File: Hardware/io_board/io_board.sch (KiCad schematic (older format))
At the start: 31 parts, among them J1 Conn_01x40, J2 Conn_02x05_Odd_Even, J3 Mini-DIN-6, J4 Conn_02x10_Odd_Even, U1 74LS138, U2 W65C22NxP, U3 74LS14

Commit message: Make IO board through hole
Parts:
- removed J2: Conn_02x05_Odd_Even, Connector_PinHeader_2.54mm:PinHeader_2x07_P2.54mm_Horizontal, symbol Connector_Generic:Conn_02x07_Odd_Even
- added J2: Conn_02x06_Odd_Even, Connector_PinHeader_2.54mm:PinHeader_2x06_P2.54mm_Horizontal, symbol Connector_Generic:Conn_02x06_Odd_Even
- C1, C2, C3, C4: value C_Small -> 4.7u; footprint Capacitor_SMD:C_1206_3216Metric_Pad1.42x1.75mm_HandSolder -> Capacitor_THT:C_Disc_D4.7mm_W2.5mm_P5.00mm
- D1, D2, D3, D4, D5, D6, D7, D8: footprint LED_SMD:LED_1206_3216Metric_Pad1.42x1.75mm_HandSolder -> LED_THT:LED_D3.0mm_Horizontal_O3.81mm_Z6.0mm
- R1, R10, R11, R12, R2, R3, R4, R5, R6, R7, R8, R9: footprint Resistor_SMD:R_0805_2012Metric_Pad1.15x1.40mm_HandSolder -> Resistor_THT:R_Axial_DIN0204_L3.6mm_D1.6mm_P5.08mm_Horizontal
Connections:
- net +5V: now also J2.2 (Pin_2)
- net CA1: now also J2.6 (Pin_6)
- net CA2: now also J2.4 (Pin_4)
- net GND: now also C2.2, J2.8 (Pin_8)
- net PA0: now also J2.11 (Pin_11)
- net PA1: now also J2.9 (Pin_9)
- net PA2: now also J2.7 (Pin_7)
- net PA3: now also J2.5 (Pin_5)
- net PA4: now also J2.3 (Pin_3)
- net PA5: now also J2.1 (Pin_1)
- net PA6: now also J2.12 (Pin_12)
- net PA7: now also J2.10 (Pin_10)
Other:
- moved on the sheet: U3F

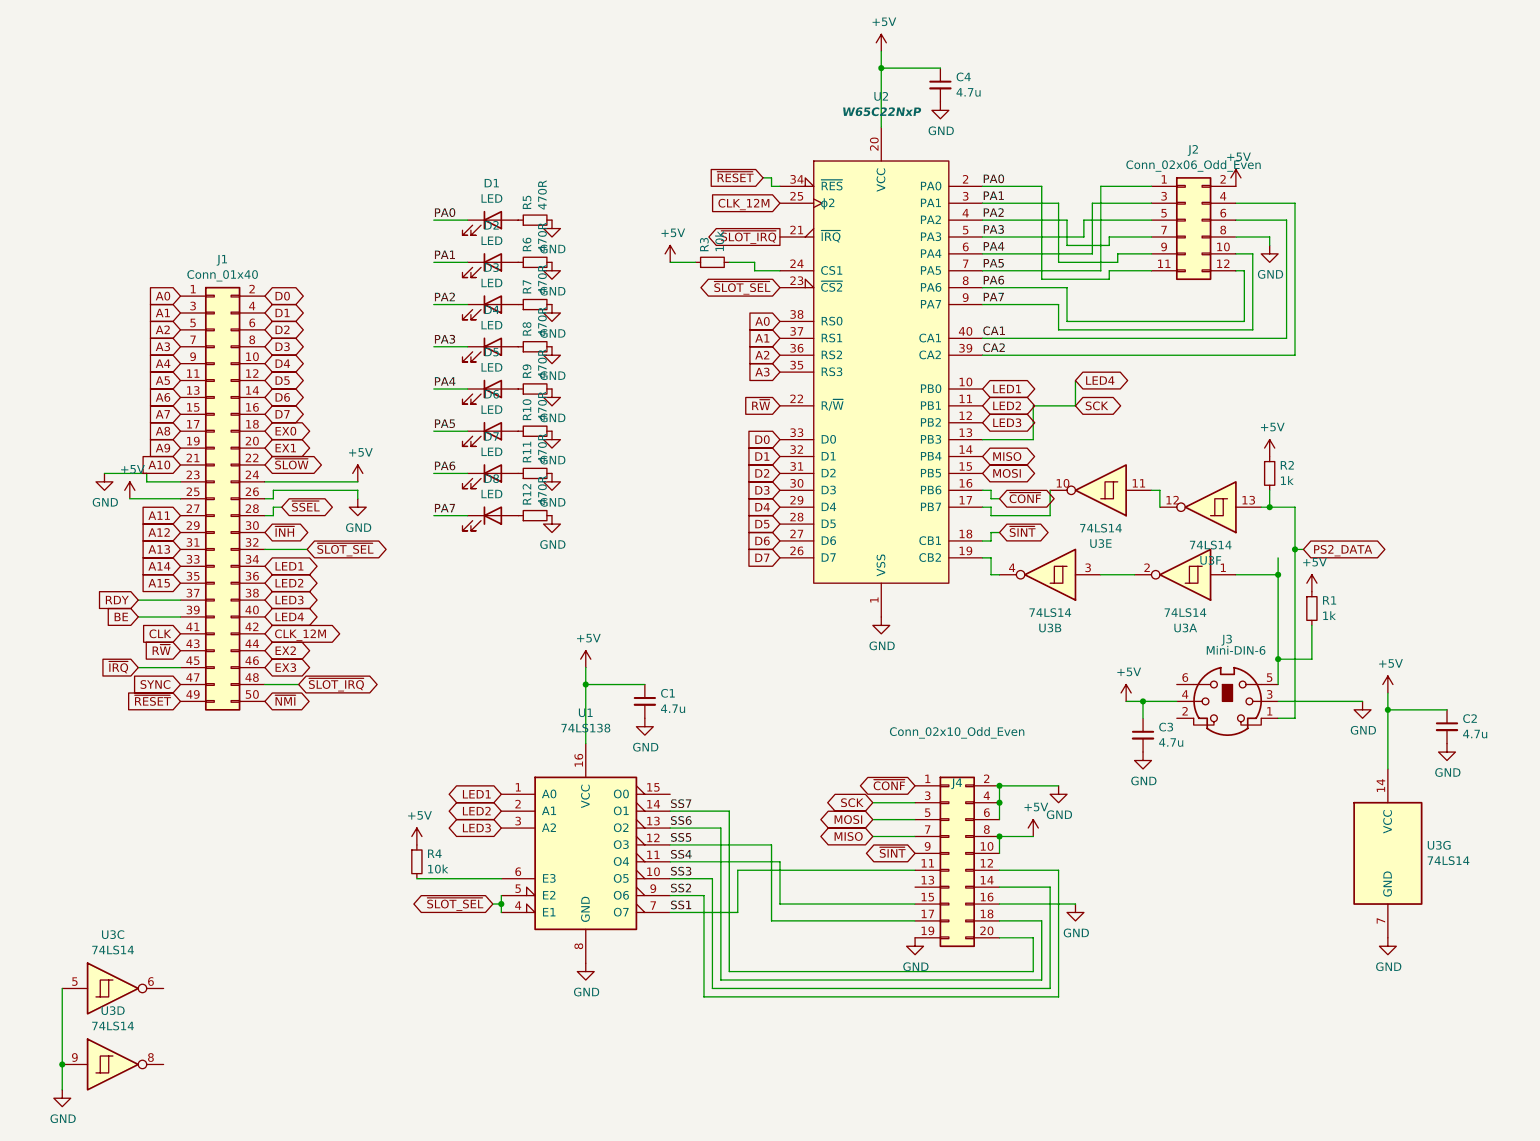
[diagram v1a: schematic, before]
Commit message: final update for through hole conversion
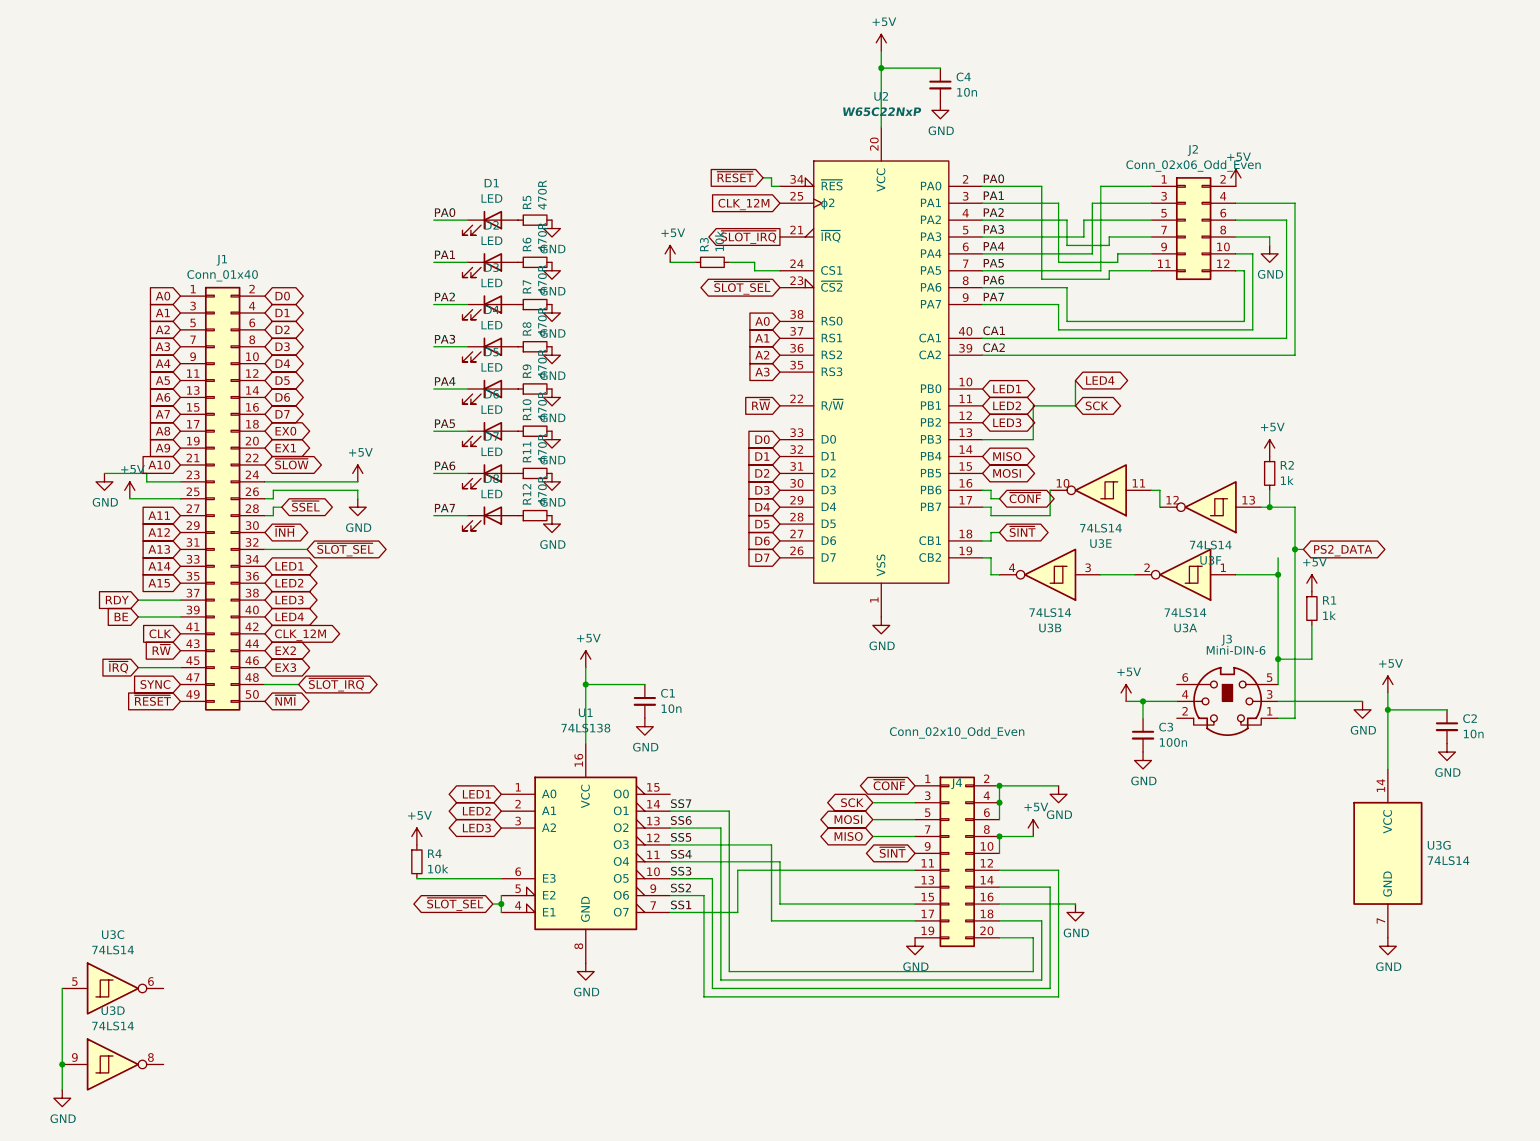
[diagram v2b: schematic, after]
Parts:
- C1, C2, C4: value 4.7u -> 10n
- C3: value 4.7u -> 100n
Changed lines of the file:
@@
 P 6800 1000
 F 0 "C4" H 6892 1046 50  0000 L CNN
-F 1 "4.7u" H 6892 955 50  0000 L CNN
+F 1 "10n" H 6892 955 50  0000 L CNN
 F 2 "Capacitor_THT:C_Disc_D4.7mm_W2.5mm_P5.00mm" H 6800 1000 50  0001 C CNN
 F 3 "~" H 6800 1000 50  0001 C CNN
@@
 P 5050 4650
 F 0 "C1" H 5142 4696 50  0000 L CNN
-F 1 "4.7u" H 5142 4605 50  0000 L CNN
+F 1 "10n" H 5142 4605 50  0000 L CNN
 F 2 "Capacitor_THT:C_Disc_D4.7mm_W2.5mm_P5.00mm" H 5050 4650 50  0001 C CNN
 F 3 "~" H 5050 4650 50  0001 C CNN
@@
 P 9800 4800
 F 0 "C2" H 9892 4846 50  0000 L CNN
-F 1 "4.7u" H 9892 4755 50  0000 L CNN
+F 1 "10n" H 9892 4755 50  0000 L CNN
 F 2 "Capacitor_THT:C_Disc_D4.7mm_W2.5mm_P5.00mm" H 9800 4800 50  0001 C CNN
 F 3 "~" H 9800 4800 50  0001 C CNN
@@
 P 8000 4850
 F 0 "C3" H 8092 4896 50  0000 L CNN
-F 1 "4.7u" H 8092 4805 50  0000 L CNN
+F 1 "100n" H 8092 4805 50  0000 L CNN
 F 2 "Capacitor_THT:C_Disc_D4.7mm_W2.5mm_P5.00mm" H 8000 4850 50  0001 C CNN
 F 3 "~" H 8000 4850 50  0001 C CNN

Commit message: update io board with bigger resistors
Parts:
- R1, R10, R11, R12, R2, R3, R4, R5, R6, R7, R8, R9: footprint Resistor_THT:R_Axial_DIN0204_L3.6mm_D1.6mm_P5.08mm_Horizontal -> Resistor_THT:R_Axial_DIN0207_L6.3mm_D2.5mm_P7.62mm_Horizontal
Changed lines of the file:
@@
 F 0 "R2" H 8809 3346 50  0000 L CNN
 F 1 "1k" H 8809 3255 50  0000 L CNN
-F 2 "Resistor_THT:R_Axial_DIN0204_L3.6mm_D1.6mm_P5.08mm_Horizontal" H 8750 3300 50  0001 C CNN
+F 2 "Resistor_THT:R_Axial_DIN0207_L6.3mm_D2.5mm_P7.62mm_Horizontal" H 8750 3300 50  0001 C CNN
 F 3 "~" H 8750 3300 50  0001 C CNN
 	1    8750 3300
@@
 F 0 "R1" H 9059 4146 50  0000 L CNN
 F 1 "1k" H 9059 4055 50  0000 L CNN
-F 2 "Resistor_THT:R_Axial_DIN0204_L3.6mm_D1.6mm_P5.08mm_Horizontal" H 9000 4100 50  0001 C CNN
+F 2 "Resistor_THT:R_Axial_DIN0207_L6.3mm_D2.5mm_P7.62mm_Horizontal" H 9000 4100 50  0001 C CNN
 F 3 "~" H 9000 4100 50  0001 C CNN
 	1    9000 4100
@@
 F 0 "R3" H 5509 2096 50  0000 L CNN
 F 1 "10k" H 5509 2005 50  0000 L CNN
-F 2 "Resistor_THT:R_Axial_DIN0204_L3.6mm_D1.6mm_P5.08mm_Horizontal" H 5450 2050 50  0001 C CNN
+F 2 "Resistor_THT:R_Axial_DIN0207_L6.3mm_D2.5mm_P7.62mm_Horizontal" H 5450 2050 50  0001 C CNN
 F 3 "~" H 5450 2050 50  0001 C CNN
 	1    5450 2050
@@
 F 0 "R4" H 3759 5646 50  0000 L CNN
 F 1 "10k" H 3759 5555 50  0000 L CNN
-F 2 "Resistor_THT:R_Axial_DIN0204_L3.6mm_D1.6mm_P5.08mm_Horizontal" H 3700 5600 50  0001 C CNN
+F 2 "Resistor_THT:R_Axial_DIN0207_L6.3mm_D2.5mm_P7.62mm_Horizontal" H 3700 5600 50  0001 C CNN
 F 3 "~" H 3700 5600 50  0001 C CNN
 	1    3700 5600
@@
 F 0 "R5" H 4459 1846 50  0000 L CNN
 F 1 "470R" H 4459 1755 50  0000 L CNN
-F 2 "Resistor_THT:R_Axial_DIN0204_L3.6mm_D1.6mm_P5.08mm_Horizontal" H 4400 1800 50  0001 C CNN
+F 2 "Resistor_THT:R_Axial_DIN0207_L6.3mm_D2.5mm_P7.62mm_Horizontal" H 4400 1800 50  0001 C CNN
 F 3 "~" H 4400 1800 50  0001 C CNN
 	1    4400 1800
@@
 F 0 "R6" H 4459 2096 50  0000 L CNN
 F 1 "470R" H 4459 2005 50  0000 L CNN
-F 2 "Resistor_THT:R_Axial_DIN0204_L3.6mm_D1.6mm_P5.08mm_Horizontal" H 4400 2050 50  0001 C CNN
+F 2 "Resistor_THT:R_Axial_DIN0207_L6.3mm_D2.5mm_P7.62mm_Horizontal" H 4400 2050 50  0001 C CNN
 F 3 "~" H 4400 2050 50  0001 C CNN
 	1    4400 2050
@@
 F 0 "R7" H 4459 2346 50  0000 L CNN
 F 1 "470R" H 4459 2255 50  0000 L CNN
-F 2 "Resistor_THT:R_Axial_DIN0204_L3.6mm_D1.6mm_P5.08mm_Horizontal" H 4400 2300 50  0001 C CNN
+F 2 "Resistor_THT:R_Axial_DIN0207_L6.3mm_D2.5mm_P7.62mm_Horizontal" H 4400 2300 50  0001 C CNN
 F 3 "~" H 4400 2300 50  0001 C CNN
 	1    4400 2300
@@
 F 0 "R8" H 4459 2596 50  0000 L CNN
 F 1 "470R" H 4459 2505 50  0000 L CNN
-F 2 "Resistor_THT:R_Axial_DIN0204_L3.6mm_D1.6mm_P5.08mm_Horizontal" H 4400 2550 50  0001 C CNN
+F 2 "Resistor_THT:R_Axial_DIN0207_L6.3mm_D2.5mm_P7.62mm_Horizontal" H 4400 2550 50  0001 C CNN
 F 3 "~" H 4400 2550 50  0001 C CNN
 	1    4400 2550
@@
 F 0 "R9" H 4459 2846 50  0000 L CNN
 F 1 "470R" H 4459 2755 50  0000 L CNN
-F 2 "Resistor_THT:R_Axial_DIN0204_L3.6mm_D1.6mm_P5.08mm_Horizontal" H 4400 2800 50  0001 C CNN
+F 2 "Resistor_THT:R_Axial_DIN0207_L6.3mm_D2.5mm_P7.62mm_Horizontal" H 4400 2800 50  0001 C CNN
 F 3 "~" H 4400 2800 50  0001 C CNN
 	1    4400 2800
@@
 F 0 "R10" H 4459 3096 50  0000 L CNN
 F 1 "470R" H 4459 3005 50  0000 L CNN
-F 2 "Resistor_THT:R_Axial_DIN0204_L3.6mm_D1.6mm_P5.08mm_Horizontal" H 4400 3050 50  0001 C CNN
+F 2 "Resistor_THT:R_Axial_DIN0207_L6.3mm_D2.5mm_P7.62mm_Horizontal" H 4400 3050 50  0001 C CNN
 F 3 "~" H 4400 3050 50  0001 C CNN
 	1    4400 3050
@@
 F 0 "R11" H 4459 3346 50  0000 L CNN
 F 1 "470R" H 4459 3255 50  0000 L CNN
-F 2 "Resistor_THT:R_Axial_DIN0204_L3.6mm_D1.6mm_P5.08mm_Horizontal" H 4400 3300 50  0001 C CNN
+F 2 "Resistor_THT:R_Axial_DIN0207_L6.3mm_D2.5mm_P7.62mm_Horizontal" H 4400 3300 50  0001 C CNN
 F 3 "~" H 4400 3300 50  0001 C CNN
 	1    4400 3300
@@
 F 0 "R12" H 4459 3596 50  0000 L CNN
 F 1 "470R" H 4459 3505 50  0000 L CNN
-F 2 "Resistor_THT:R_Axial_DIN0204_L3.6mm_D1.6mm_P5.08mm_Horizontal" H 4400 3550 50  0001 C CNN
+F 2 "Resistor_THT:R_Axial_DIN0207_L6.3mm_D2.5mm_P7.62mm_Horizontal" H 4400 3550 50  0001 C CNN
 F 3 "~" H 4400 3550 50  0001 C CNN
 	1    4400 3550

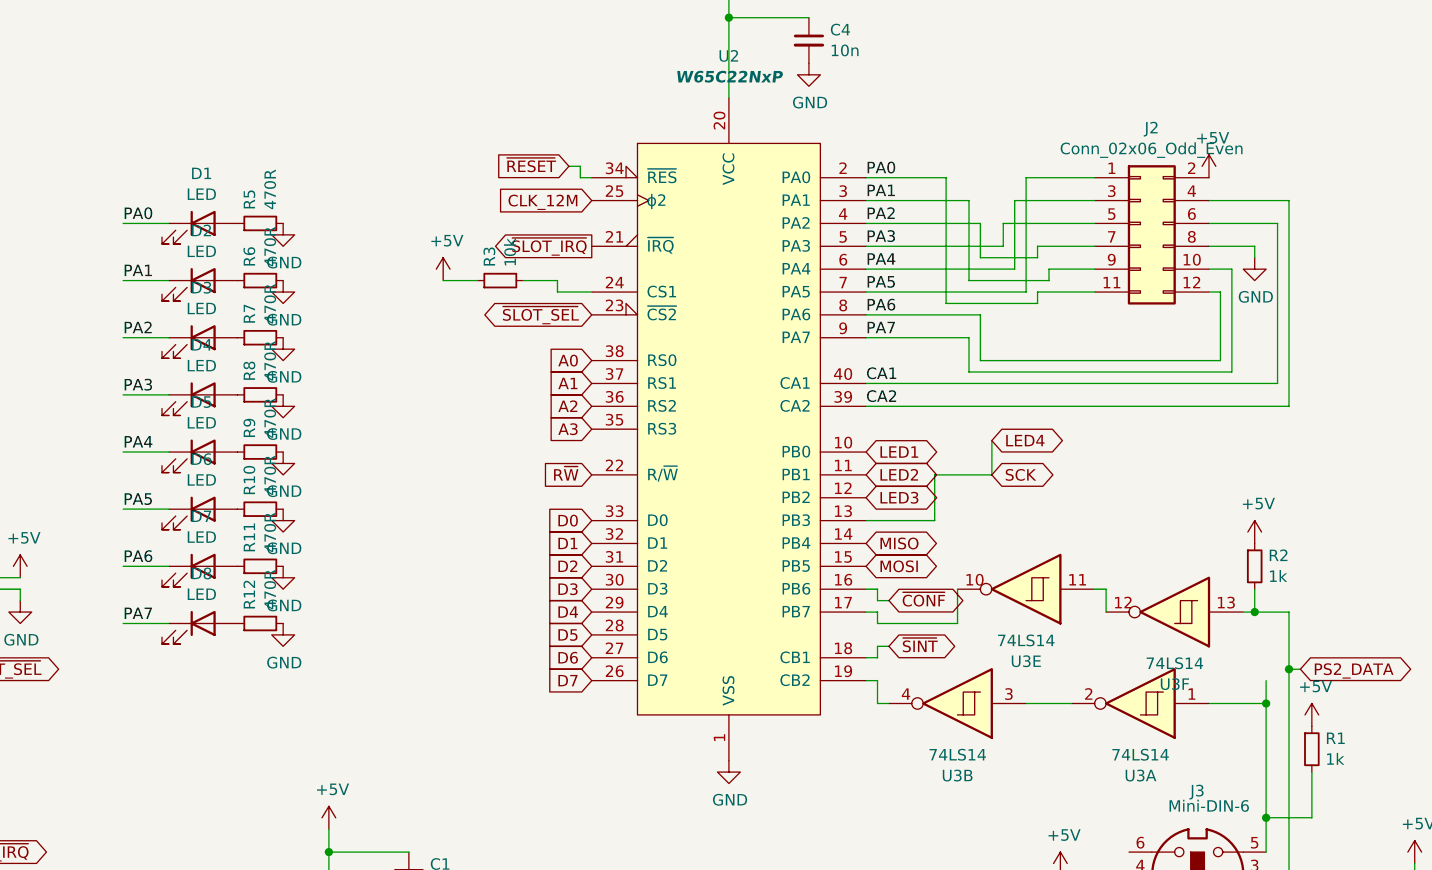
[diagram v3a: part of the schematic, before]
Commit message: Fix LED orientation + move resistor under socket
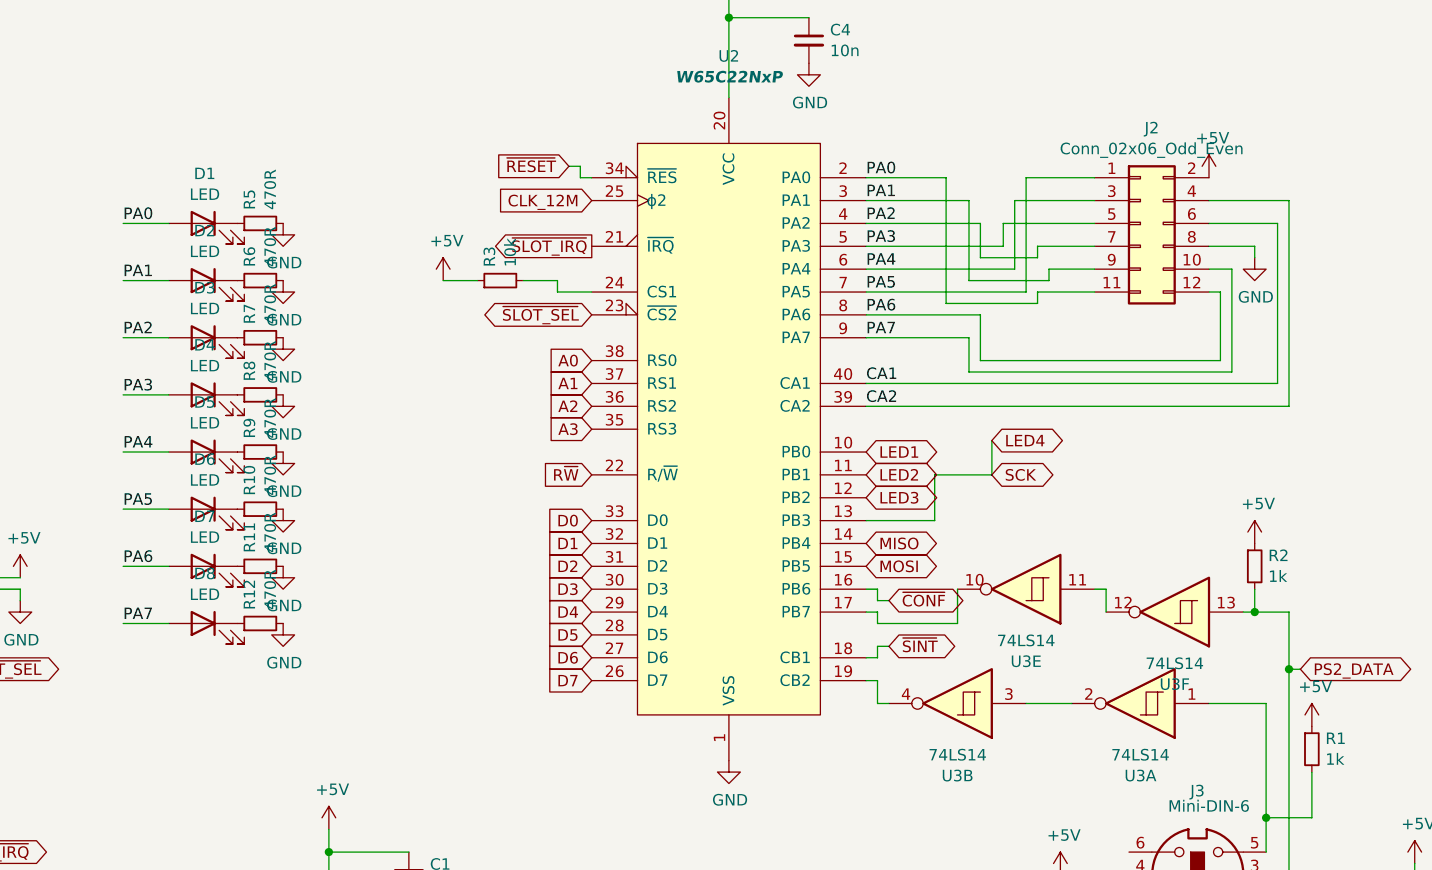
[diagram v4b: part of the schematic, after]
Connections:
- net PA0: now also D1.2 (A); no longer D1.1 (K)
- net PA1: now also D2.2 (A); no longer D2.1 (K)
- net PA2: now also D3.2 (A); no longer D3.1 (K)
- net PA3: now also D4.2 (A); no longer D4.1 (K)
- net PA4: now also D5.2 (A); no longer D5.1 (K)
- net PA5: now also D6.2 (A); no longer D6.1 (K)
- net PA6: now also D7.2 (A); no longer D7.1 (K)
- net PA7: now also D8.2 (A); no longer D8.1 (K)
- net at R5.1: now also D1.1 (K); no longer D1.2 (A)
- net at R6.1: now also D2.1 (K); no longer D2.2 (A)
- net at R7.1: now also D3.1 (K); no longer D3.2 (A)
- net at R8.1: now also D4.1 (K); no longer D4.2 (A)
- net at R9.1: now also D5.1 (K); no longer D5.2 (A)
- net at R10.1: now also D6.1 (K); no longer D6.2 (A)
- net at R11.1: now also D7.1 (K); no longer D7.2 (A)
- net at R12.1: now also D8.1 (K); no longer D8.2 (A)
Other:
- moved on the sheet: D1, D2, D3, D4, D5, D6, D7, D8
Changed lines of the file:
@@
 F 3 "~" H 4150 1800 50  0001 C CNN
 	1    4150 1800
-	1    0    0    -1
+	-1   0    0    -1
 $EndComp
 $Comp
@@
 F 3 "~" H 4150 2050 50  0001 C CNN
 	1    4150 2050
-	1    0    0    -1
+	-1   0    0    -1
 $EndComp
 $Comp
@@
 F 3 "~" H 4150 2300 50  0001 C CNN
 	1    4150 2300
-	1    0    0    -1
+	-1   0    0    -1
 $EndComp
 $Comp
@@
 F 3 "~" H 4150 2550 50  0001 C CNN
 	1    4150 2550
-	1    0    0    -1
+	-1   0    0    -1
 $EndComp
 $Comp
@@
 F 3 "~" H 4150 2800 50  0001 C CNN
 	1    4150 2800
-	1    0    0    -1
+	-1   0    0    -1
 $EndComp
 $Comp
@@
 F 3 "~" H 4150 3050 50  0001 C CNN
 	1    4150 3050
-	1    0    0    -1
+	-1   0    0    -1
 $EndComp
 $Comp
@@
 F 3 "~" H 4150 3300 50  0001 C CNN
 	1    4150 3300
-	1    0    0    -1
+	-1   0    0    -1
 $EndComp
 $Comp
@@
 F 3 "~" H 4150 3550 50  0001 C CNN
 	1    4150 3550
-	1    0    0    -1
+	-1   0    0    -1
 $EndComp
 $Comp
@@
 Wire Wire Line
 	8550 3900 8800 3900
-Connection ~ 8800 3900
-Wire Wire Line
-	8800 3900 8800 3800
 Wire Wire Line
 	7950 3900 7750 3900
